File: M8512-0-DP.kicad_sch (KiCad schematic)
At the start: 1 part, among them J1 KL10_6-bay_backplane_connector

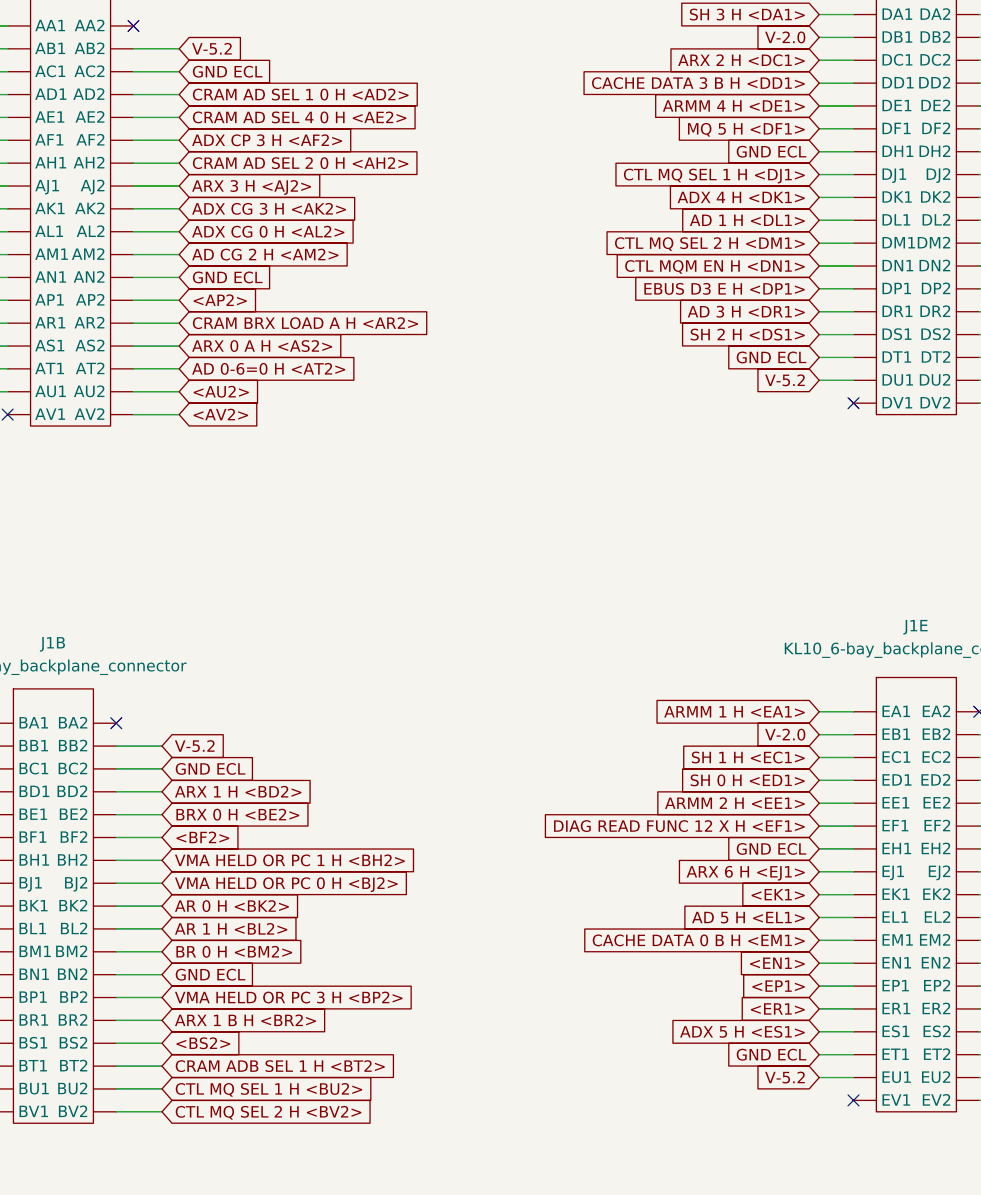
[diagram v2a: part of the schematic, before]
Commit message: Fix a bunch of typos and their backplane signal names
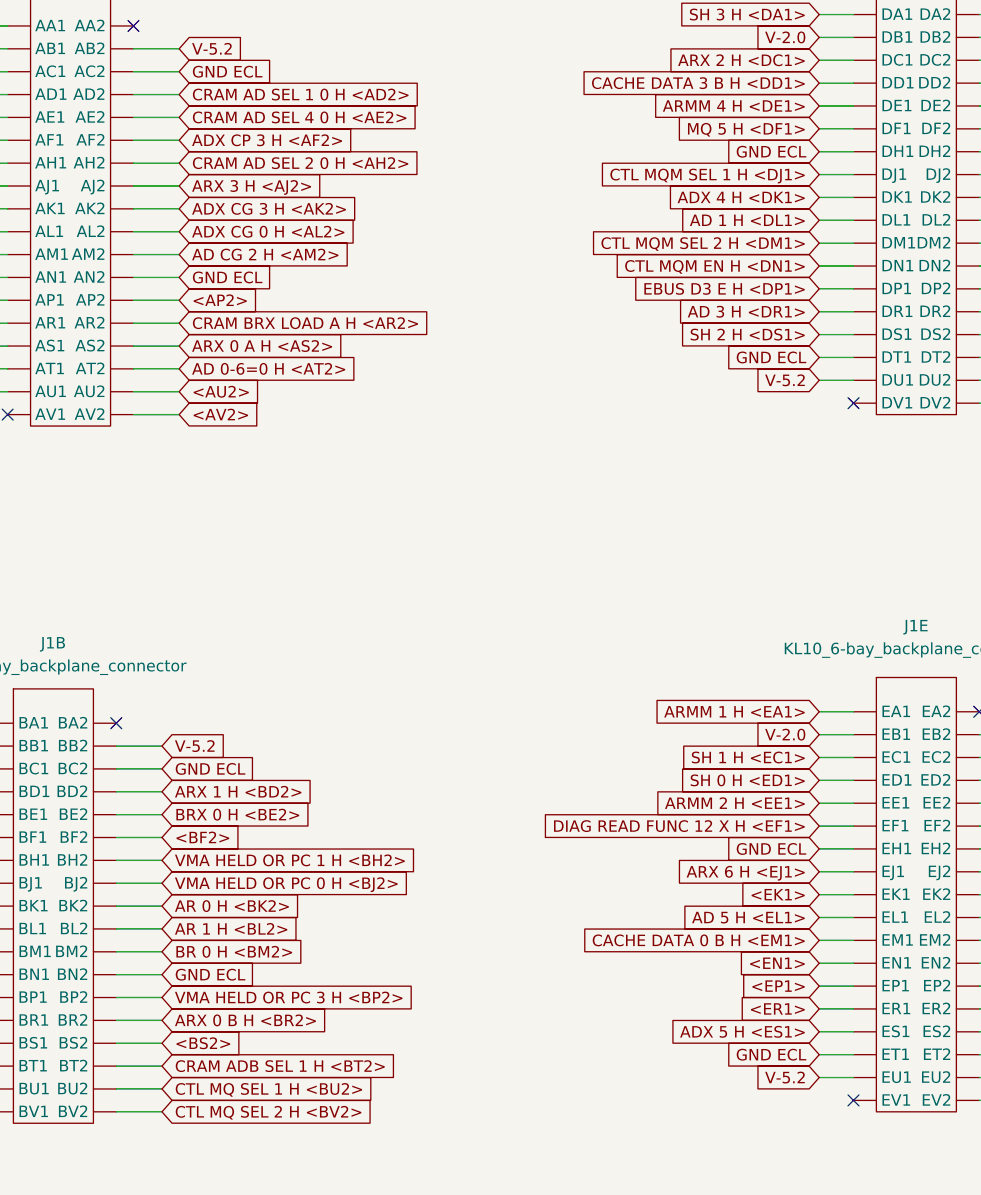
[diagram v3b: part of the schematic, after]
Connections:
- net ARX 1 B H <BR2> renamed ARX 0 B H <BR2>
- net CTL MQ SEL 1 H <DJ1> renamed CTL MQM SEL 1 H <DJ1>
- net CTL MQ SEL 2 H <DM1> renamed CTL MQM SEL 2 H <DM1>
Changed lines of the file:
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@@
     )
   )
-  (global_label "CTL MQ SEL 1 H <DJ1>" (shape input) (at 304.8 48.895 180) (fields_autoplaced)
-    (effects (font (size 1.27 1.27)) (justify right))
-    (property "Intersheet References" "${INTERSHEET_REFS}" (id 0) (at 278.9826 48.8156 0)
+  (global_label "CTL MQM SEL 1 H <DJ1>" (shape input) (at 304.8 48.895 180) (fields_autoplaced)
+    (effects (font (size 1.27 1.27)) (justify right))
+    (property "Intersheet References" "${INTERSHEET_REFS}" (id 0) (at 277.5312 48.8156 0)
       (effects (font (size 1.27 1.27)) (justify right) hide)
     )
@@
     )
   )
-  (global_label "CTL MQ SEL 2 H <DM1>" (shape input) (at 304.8 56.515 180) (fields_autoplaced)
-    (effects (font (size 1.27 1.27)) (justify right))
-    (property "Intersheet References" "${INTERSHEET_REFS}" (id 0) (at 278.4988 56.4356 0)
+  (global_label "CTL MQM SEL 2 H <DM1>" (shape input) (at 304.8 56.515 180) (fields_autoplaced)
+    (effects (font (size 1.27 1.27)) (justify right))
+    (property "Intersheet References" "${INTERSHEET_REFS}" (id 0) (at 277.0474 56.4356 0)
       (effects (font (size 1.27 1.27)) (justify right) hide)
     )
@@
     )
   )
-  (global_label "ARX 1 B H <BR2>" (shape input) (at 231.775 142.875 0) (fields_autoplaced)
+  (global_label "ARX 0 B H <BR2>" (shape input) (at 231.775 142.875 0) (fields_autoplaced)
     (effects (font (size 1.27 1.27)) (justify left))
     (property "Intersheet References" "${INTERSHEET_REFS}" (id 0) (at 252.331 142.7956 0)

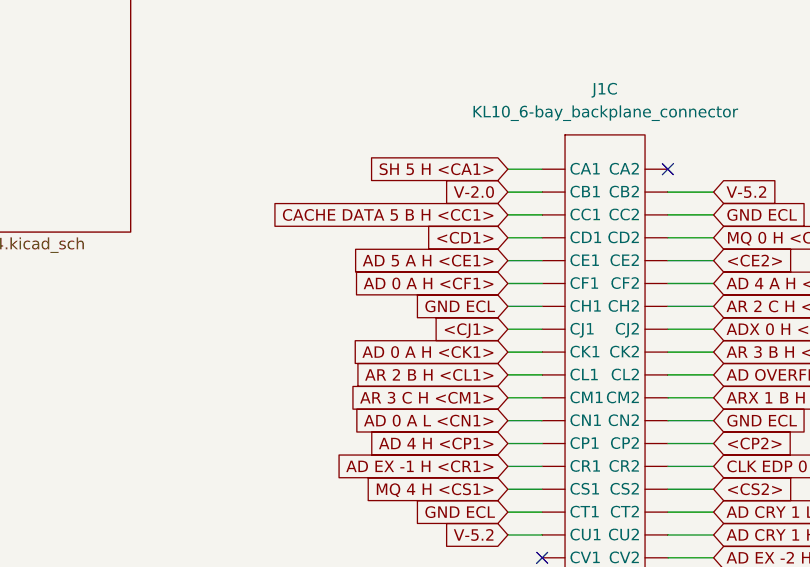
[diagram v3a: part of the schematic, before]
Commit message: Add tool to convert schematic to JSON
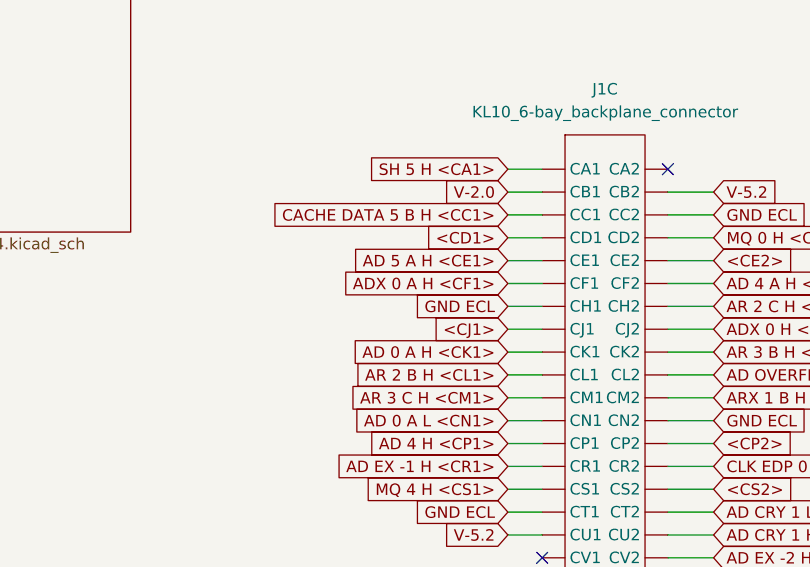
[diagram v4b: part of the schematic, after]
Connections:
- net AD 0 A H <CF1> renamed ADX 0 A H <CF1>
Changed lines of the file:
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@@
     (comment 1 "M8512-0-DP")
   )
-  (bus_alias "CACHE_DATA[0..5]" (members ))
+  (bus_alias "BR[0..5]" (members ))
+  (bus_alias "ARMM[0..5]" (members ))
+  (bus_alias "-CRAM_ADA_DIS[0..5]L" (members ))
+  (bus_alias "VMA_HELD_OR_PC[0..5]" (members ))
+  (bus_alias "EBUS_D[0..5]" (members ))
+  (bus_alias "APR_FM_BLOCK" (members ))
+  (bus_alias "CRAM_ADA_SEL[2..1]" (members ))
+  (bus_alias "#[0..5]" (members "4" "2" "1"))
+  (bus_alias "ADA[0..5]" (members ))
+  (bus_alias "AD_CP[0..5]" (members ))
+  (bus_alias "AD_CG[0..5]" (members ))
+  (bus_alias "AR[0..5]" (members ))
+  (bus_alias "SH[0..5]" (members ))
   (bus_alias "AD_CRY_[0..5]" (members ))
   (bus_alias "FM[0..5]" (members ))
-  (bus_alias "-AD[0.5]-[5..10]=0" (members ))
-  (bus_alias "SH[0..5]" (members ))
-  (bus_alias "ADA[0..5]" (members ))
-  (bus_alias "#[0..5]" (members "4" "2" "1"))
-  (bus_alias "CRAM_ADA_SEL[2..1]" (members ))
-  (bus_alias "EBUS_D[0..5]" (members ))
-  (bus_alias "AD_CG[0..5]" (members ))
-  (bus_alias "AR[0..5]" (members ))
-  (bus_alias "-CRAM_ADA_DIS[0..5]L" (members ))
-  (bus_alias "ARMM[0..5]" (members ))
-  (bus_alias "APR_FM_ADR" (members "10" "4" "2" "1"))
+  (bus_alias "MQ[0..5]" (members ))
+  (bus_alias "CACHE_DATA[0..5]" (members ))
   (bus_alias "AD[0..5]" (members ))
   (bus_alias "DIAG[4..6]" (members ))
   (bus_alias "BRX[0..5]" (members ))
-  (bus_alias "MQ[0..5]" (members ))
   (bus_alias "ADX_CG[0..5]" (members ))
+  (bus_alias "-AD[0.5]-[5..10]=0" (members ))
   (bus_alias "CRAM_ADB_SEL[2..1]" (members ))
+  (bus_alias "MQM[0..5]" (members ))
   (bus_alias "EDP_FM_PARITY[0..5]-[5..10]" (members ))
+  (bus_alias "ADXA[0..5]" (members ))
   (bus_alias "ADX[0..5]" (members ))
+  (bus_alias "APR_FM_ADR" (members "10" "4" "2" "1"))
+  (bus_alias "ADB[0..5]" (members "8" "4" "2" "1" "BOOLE"))
   (bus_alias "ADX_CP[0..5]" (members ))
-  (bus_alias "MQM[0..5]" (members ))
-  (bus_alias "ADB[0..5]" (members "8" "4" "2" "1" "BOOLE"))
-  (bus_alias "ADXA[0..5]" (members ))
-  (bus_alias "APR_FM_BLOCK" (members ))
   (bus_alias "ADXB[0..5]" (members ))
-  (bus_alias "AD_CP[0..5]" (members ))
-  (bus_alias "VMA_HELD_OR_PC[0..5]" (members ))
-  (bus_alias "BR[0..5]" (members ))
   (no_connect (at 214.63 75.565))
   (no_connect (at 322.58 108.585))
@@
     )
   )
-  (global_label "AD 0 A H <CF1>" (shape input) (at 208.915 195.58 180) (fields_autoplaced)
-    (effects (font (size 1.27 1.27)) (justify right))
-    (property "Intersheet References" "${INTERSHEET_REFS}" (id 0) (at 189.9314 195.5006 0)
-      (effects (font (size 1.27 1.27)) (justify right) hide)
-    )
+  (global_label "ADX 0 A H <CF1>" (shape input) (at 208.915 195.58 180) (fields_autoplaced)
+    (effects (font (size 1.27 1.27)) (justify right))
+    (property "Intersheet References" "${INTERSHEET_REFS}" (id 0) (at 188.7219 195.5006 0)
+      (effects (font (size 1.27 1.27)) (justify right) hide)
+    )
